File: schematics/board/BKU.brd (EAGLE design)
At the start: 94 x 94 mm, 71 parts, among them Q1 8MHz, Q2 32,768KHz, U1 STM32F405RGT6

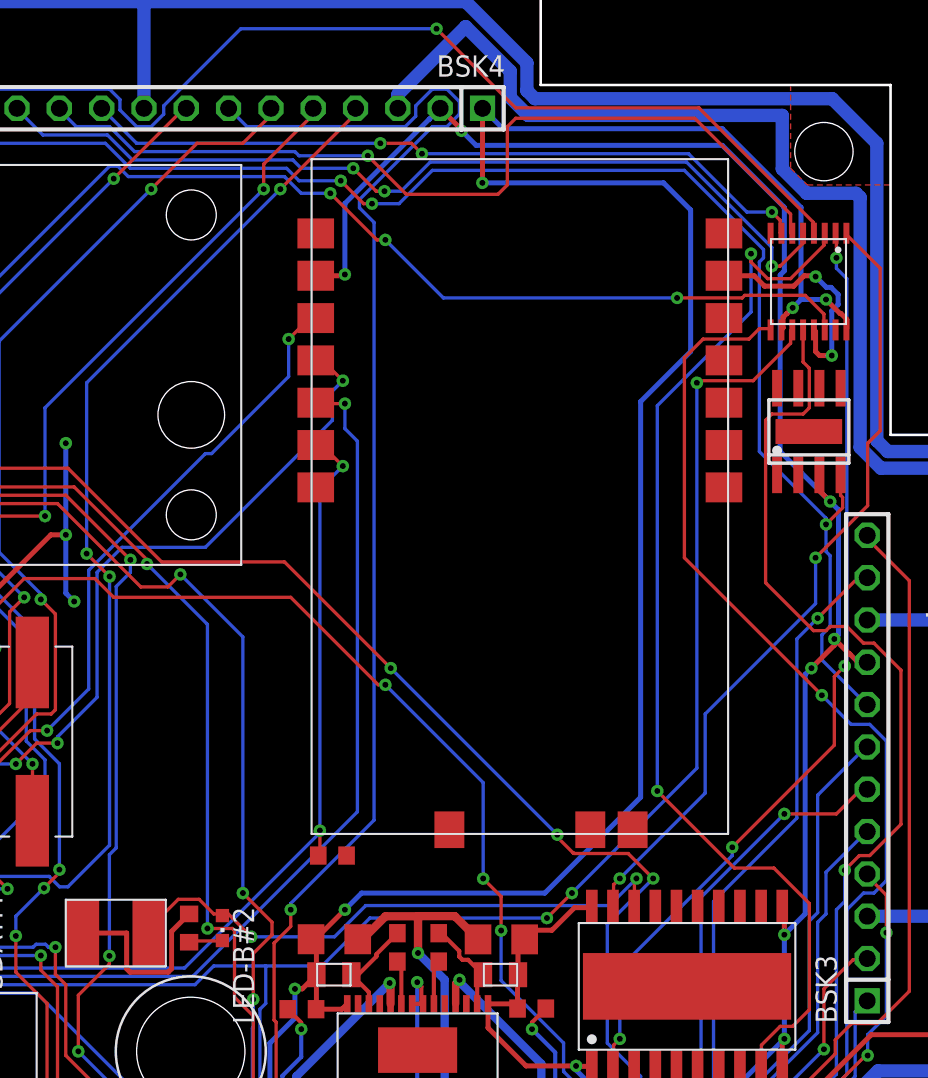
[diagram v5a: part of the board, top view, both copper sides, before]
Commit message: Исправлены RADIO и диоды
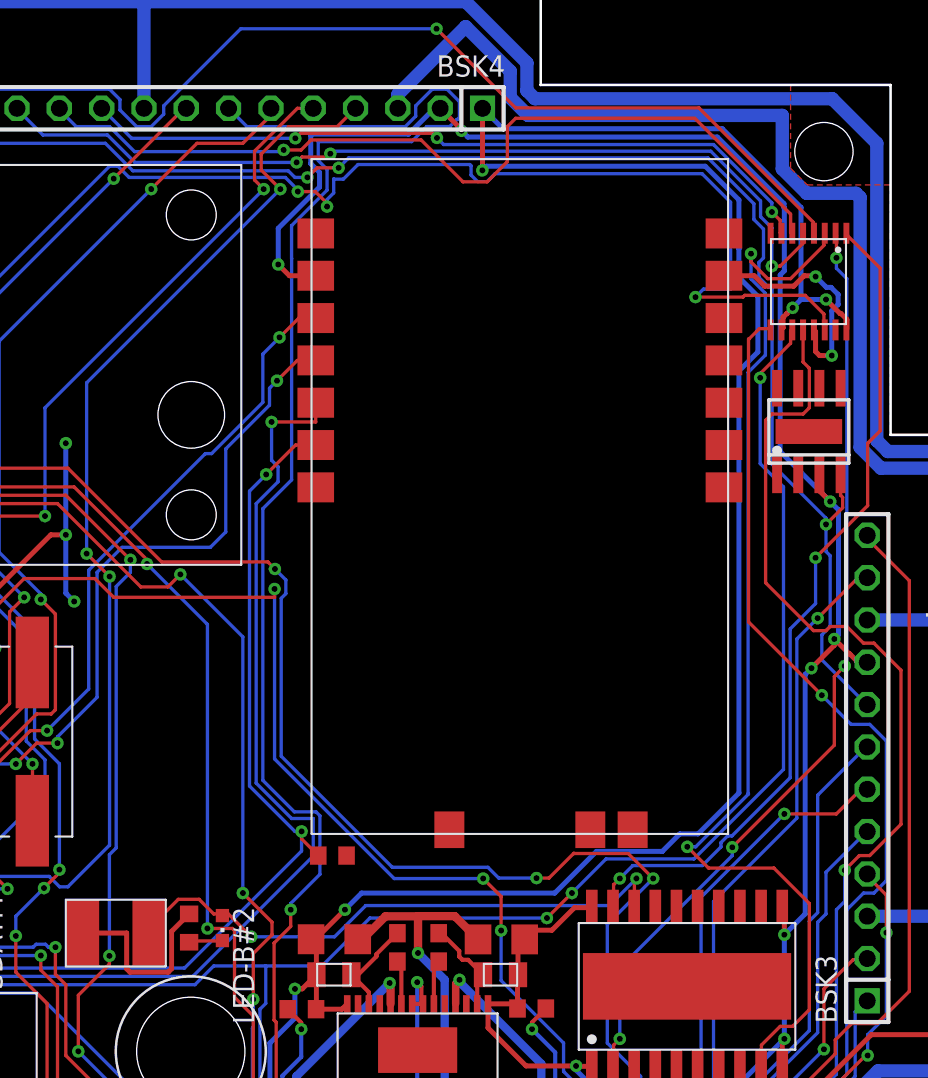
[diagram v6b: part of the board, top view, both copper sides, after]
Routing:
- net DS: track 111.3 -> 122.2 mm
- net VDD: track 457.2 -> 465.7 mm
- net B2A_KEM+: track 119.5 -> 127.3 mm
- net SCLTM: track 137.6 -> 144.6 mm
- net 5V: track 237.7 -> 243.6 mm
- net N$17: track 84.6 -> 79.8 mm
- net SDA: track 84.4 -> 87.8 mm
- net TIME: track 119.5 -> 122.2 mm
- net B1_KHEAT: track 47.9 -> 50.5 mm
- net SHCP: track 162.1 -> 164.5 mm
- net TX-R: track 88.7 -> 91.1 mm
- net M1: track 83.9 -> 86.1 mm
- net I2CINT: track 96.9 -> 98.0 mm
- net B4_KEM+: track 53.6 -> 52.8 mm
- net RX-R: track 87.5 -> 86.7 mm
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
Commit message: Добавлены новые диоды
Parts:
- added JP1: (no value), pinheadCS:1X02
- added R14: 10k, resistor:R0603
- C14: device rcl:C1206 -> rcl:C0603
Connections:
- new net N$5: JP1.2, R14.1, U1.62
- net 5V: now also GPS.P$5
- net GND: now also R14.2
- net VDD: now also JP1.1; no longer GPS.P$5
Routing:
- net 5V: track 243.6 -> 293.3 mm, vias 12 -> 14
- net VDD: track 465.7 -> 449.1 mm, vias 22 -> 24
- net RX-ES: track 86.2 -> 95.2 mm
- net TX-ES: track 81.8 -> 89.8 mm
- net N$5: track 0.00 -> 7.13 mm
- net 1W: track 206.9 -> 210.1 mm
- net B2A_KVCC: track 134.8 -> 135.9 mm
- net B2A_KHEAT: track 120.6 -> 121.2 mm
- net GND: track 459.1 -> 459.7 mm
- net B2A_KEM-: track 115.0 -> 115.6 mm
- net N$24: track 29.2 -> 29.7 mm

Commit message: Незначительные изменения БСК1
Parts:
- C16, C17: device rcl:C1206 -> rcl:C1210
- C3: device rcl:C0603 -> rcl:C1206
- moved C3 1.03 mm to (33.1, 36.9)
- moved C16 0.46 mm to (65.8, 24.8)
- moved C17 0.40 mm to (53.5, 24.9)
- moved R8 0.05 mm to (56.1, 24.8)
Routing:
- net VDD: track 449.1 -> 450.2 mm
- net GND: track 459.7 -> 460.7 mm
- net 5V: track 293.3 -> 292.6 mm
